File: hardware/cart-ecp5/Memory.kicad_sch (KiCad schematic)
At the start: 13 parts, among them J2 MicroSD_Molex_1040310811, U3 S27KS0641DPBHI020

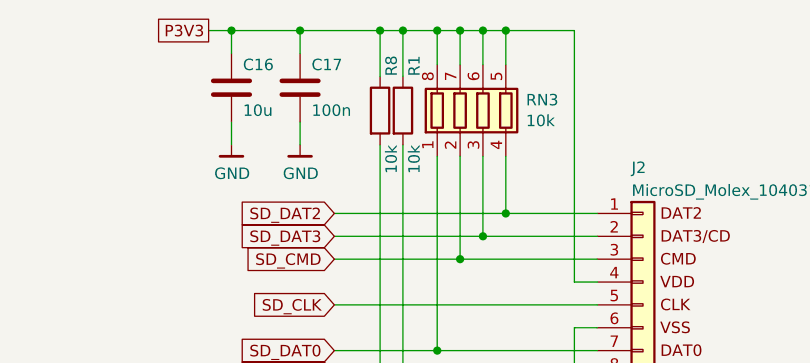
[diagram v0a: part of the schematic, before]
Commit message: hardware: Substitute library symbol for USB-C connector
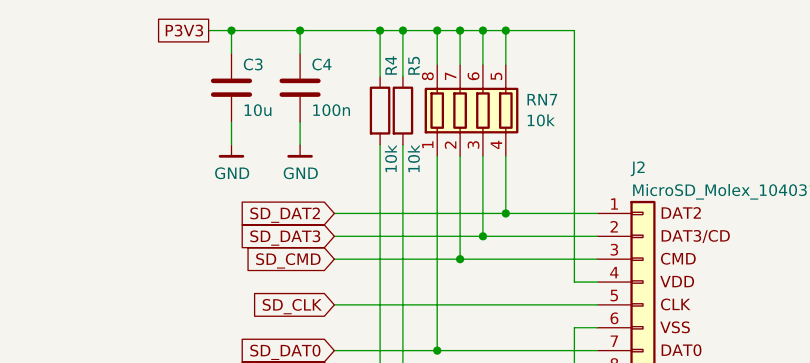
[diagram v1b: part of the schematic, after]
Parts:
- renumbered C16 to C3, C17 to C4, R8 to R4, R1 to R5, RN3 to RN7
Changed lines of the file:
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@@
 		(on_board yes)
 		(dnp no)
-		(property "Reference" "R8"
+		(property "Reference" "R4"
 			(at 193.04 76.2 90)
 			(effects
@@
 		(instances
 			(project "cart-ecp5"
-				(path "/d0de5b81-cadf-4377-8c13-b4d382700369"
-					(reference "R?")
-					(unit 1)
-				)
 				(path "/d0de5b81-cadf-4377-8c13-b4d382700369/00000000-0000-0000-0000-00005f7b735c"
 					(reference "R4")
@@
 		(on_board yes)
 		(dnp no)
-		(property "Reference" "#PWR018"
+		(property "Reference" "#PWR012"
 			(at 213.36 130.81 0)
 			(effects
@@
 		(instances
 			(project "cart-ecp5"
-				(path "/d0de5b81-cadf-4377-8c13-b4d382700369"
-					(reference "#PWR?")
-					(unit 1)
-				)
 				(path "/d0de5b81-cadf-4377-8c13-b4d382700369/00000000-0000-0000-0000-00005f7b735c"
 					(reference "#PWR012")
@@
 		(instances
 			(project "cart-ecp5"
-				(path "/d0de5b81-cadf-4377-8c13-b4d382700369"
-					(reference "J?")
-					(unit 1)
-				)
 				(path "/d0de5b81-cadf-4377-8c13-b4d382700369/00000000-0000-0000-0000-00005f7b735c"
 					(reference "J2")
@@
 		(on_board yes)
 		(dnp no)
-		(property "Reference" "R1"
+		(property "Reference" "R5"
 			(at 195.58 76.2 90)
 			(effects
@@
 		(instances
 			(project "cart-ecp5"
-				(path "/d0de5b81-cadf-4377-8c13-b4d382700369"
-					(reference "R?")
-					(unit 1)
-				)
 				(path "/d0de5b81-cadf-4377-8c13-b4d382700369/00000000-0000-0000-0000-00005f7b735c"
 					(reference "R5")
@@
 		(on_board yes)
 		(dnp no)
-		(property "Reference" "RN3"
+		(property "Reference" "RN7"
 			(at 207.9752 78.8416 0)
 			(effects
@@
 		(instances
 			(project "cart-ecp5"
-				(path "/d0de5b81-cadf-4377-8c13-b4d382700369"
-					(reference "RN?")
-					(unit 1)
-				)
 				(path "/d0de5b81-cadf-4377-8c13-b4d382700369/00000000-0000-0000-0000-00005f7b735c"
 					(reference "RN7")
@@
 		(on_board yes)
 		(dnp no)
-		(property "Reference" "C16"
+		(property "Reference" "C3"
 			(at 176.53 74.93 0)
 			(effects
@@
 		(instances
 			(project "cart-ecp5"
-				(path "/d0de5b81-cadf-4377-8c13-b4d382700369"
-					(reference "C?")
-					(unit 1)
-				)
 				(path "/d0de5b81-cadf-4377-8c13-b4d382700369/00000000-0000-0000-0000-00005f7b735c"
 					(reference "C3")
@@
 		(on_board yes)
 		(dnp no)
-		(property "Reference" "C17"
+		(property "Reference" "C4"
 			(at 184.15 74.93 0)
 			(effects
@@
 		(instances
 			(project "cart-ecp5"
-				(path "/d0de5b81-cadf-4377-8c13-b4d382700369"
-					(reference "C?")
-					(unit 1)
-				)
 				(path "/d0de5b81-cadf-4377-8c13-b4d382700369/00000000-0000-0000-0000-00005f7b735c"
 					(reference "C4")
@@
 		(on_board yes)
 		(dnp no)
-		(property "Reference" "#PWR016"
+		(property "Reference" "#PWR010"
 			(at 175.26 90.17 0)
 			(effects
@@
 		(instances
 			(project "cart-ecp5"
-				(path "/d0de5b81-cadf-4377-8c13-b4d382700369"
-					(reference "#PWR?")
-					(unit 1)
-				)
 				(path "/d0de5b81-cadf-4377-8c13-b4d382700369/00000000-0000-0000-0000-00005f7b735c"
 					(reference "#PWR010")
@@
 		(on_board yes)
 		(dnp no)
-		(property "Reference" "#PWR017"
+		(property "Reference" "#PWR011"
 			(at 182.88 90.17 0)
 			(effects
@@
 		(instances
 			(project "cart-ecp5"
-				(path "/d0de5b81-cadf-4377-8c13-b4d382700369"
-					(reference "#PWR?")
-					(unit 1)
-				)
 				(path "/d0de5b81-cadf-4377-8c13-b4d382700369/00000000-0000-0000-0000-00005f7b735c"
 					(reference "#PWR011")
